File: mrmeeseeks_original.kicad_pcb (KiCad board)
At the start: 2 copper layers, 49.6 x 62.4 mm, 23 parts, among them U1 MCP23017, X1 Badgelife_shitty_connector

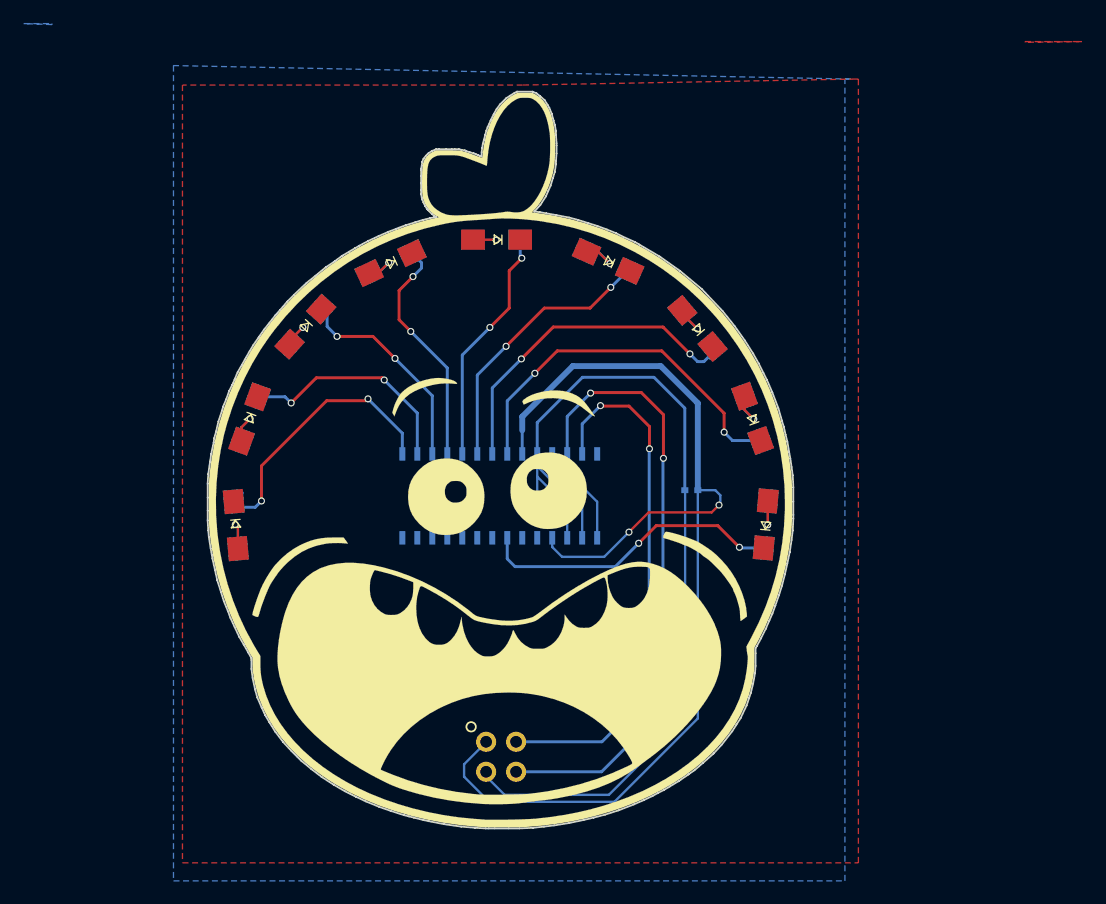
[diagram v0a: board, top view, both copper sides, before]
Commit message: Added traces to Front as Gerber2
Backup is original PCB file.
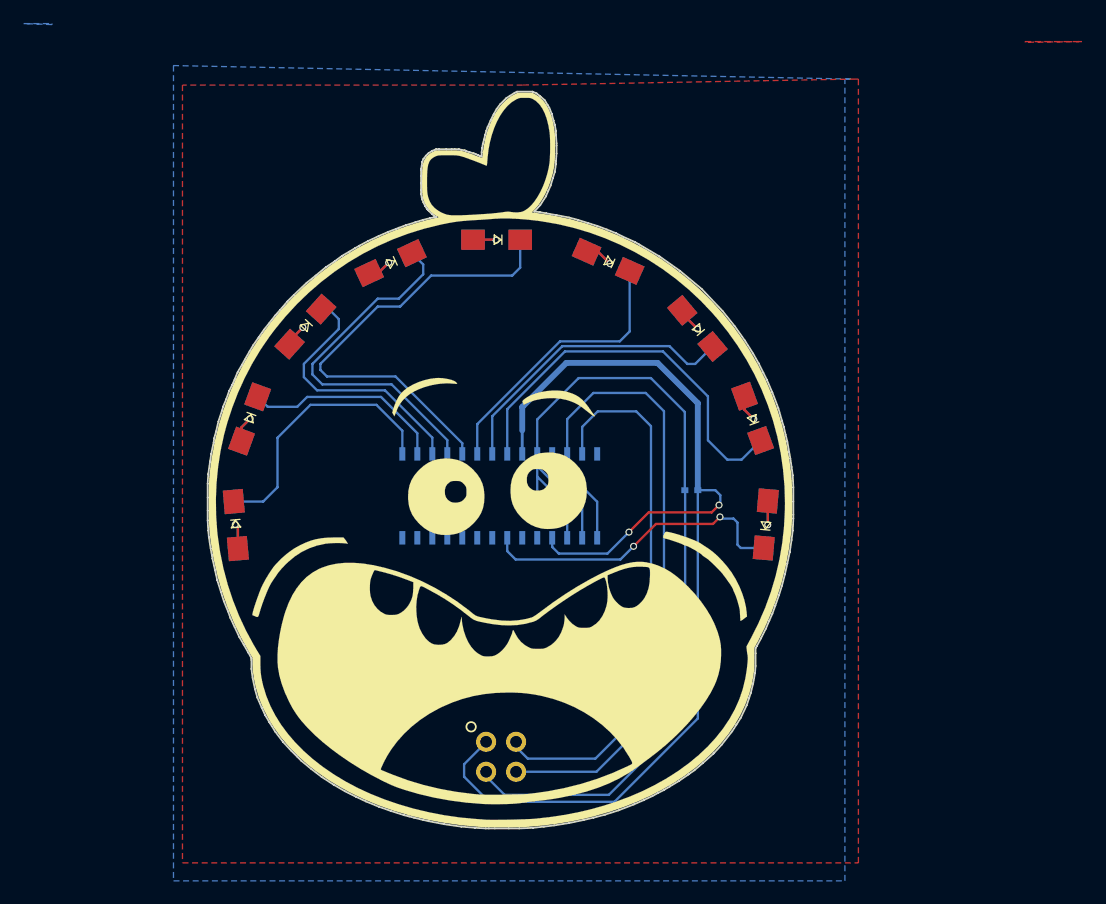
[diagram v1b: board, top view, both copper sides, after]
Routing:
- net Net-(R5-Pad1): track 20.3 -> 38.7 mm, vias 2 -> 0
- net Net-(R4-Pad1): track 21.3 -> 30.5 mm, vias 2 -> 0
- net Net-(R7-Pad1): track 30.1 -> 25.6 mm, vias 2 -> 0
- net Net-(R3-Pad1): track 19.3 -> 22.4 mm, vias 2 -> 0
- net Net-(R2-Pad1): track 20.1 -> 17.3 mm, vias 2 -> 0
- net Net-(R8-Pad1): track 31.8 -> 33.9 mm, vias 2 -> 0
- net sda: track 45.8 -> 46.9 mm, vias 2 -> 0
- net Net-(R1-Pad1): track 24.0 -> 23.0 mm, vias 2 -> 0
- net Net-(R9-Pad1): track 26.8 -> 27.6 mm
- net Net-(R6-Pad1): track 23.3 -> 23.8 mm, vias 2 -> 0
- net scl: track 52.7 -> 52.4 mm, vias 2 -> 0
